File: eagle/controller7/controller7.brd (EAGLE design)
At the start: 54.7 x 47.3 mm, 70 parts, among them U1 LM75AIM, U2 MP2307, U3 MP2307, X2 ZX62D-B-5PA8

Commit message: controller6: minor changes
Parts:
- removed H1, H2, H3, H4: MOUNT-HOLE2.8, holes:2,8
- removed J1: (no value), SparkFun-Connectors:1X02_LOCK_LONGPADS
- removed J3: (no value), SparkFun-Connectors:2X5_NOSILK
- removed RTC1: DS3231M, SparkFun-DigitalIC:SOIC8
- removed U1: LM75AIM, NSC_By_element14_Batch_1.1:SOIC127P620X175-8N
- added J4: (no value), SparkFun-Connectors:1X02_LOCK_LONGPADS
- added J7: (no value), SparkFun-Connectors:2X8
- added RTC2: DS3231M, SparkFun-DigitalIC:SOIC8
- added U$2: PIZERO_THROUGH_HOLE, pizero:PIZERO_THOUGH_HOLE
- moved J2 95.6 mm to (97.8, 52.1)
- moved J5 85.1 mm to (94.0, 45.1)
- moved Q1 85.1 mm to (95.2, 35.6)
- moved Q2 85.1 mm to (95.2, 39.4)
- moved Q3 85.1 mm to (99.1, 44.5)
- moved Q4 85.1 mm to (95.2, 31.8)
- moved R10 85.1 mm to (99.1, 35.6)
- moved R11 85.1 mm to (99.1, 38.1)
- moved R12 85.1 mm to (99.1, 40.6)
- moved R13 85.1 mm to (99.1, 33.0)
- moved R14 85.1 mm to (99.1, 30.5)
- moved J8 74.7 mm to (63.5, 54.6)
- moved S1 65.9 mm to (90.2, 61.0)
- moved R5 65.6 mm to (90.2, 55.9), turned to 0 degrees
- moved J6 65.6 mm to (63.5, 44.5)
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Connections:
- removed net N$19: U$1.2, U$1.6
- removed net VBAT: J1.1, RTC1.6
- new net N$12: U$2.2, U$2.6
- new net VBAT1: J4.1, RTC2.6
- net CONV_5V: no longer J3.1
- net GND: now also J4.2, RTC2.5; no longer J1.2, J3.5, RTC1.5, U1.4
- net N$13: no longer J3.8
- net RX: no longer J3.7
- net SCL: now also RTC2.8; no longer RTC1.8, U1.2
- net SDA: now also RTC2.7; no longer RTC1.7, U1.1
- net TX: no longer J3.9
- net VCC: now also RTC2.2; no longer RTC1.2, U1.8
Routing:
- net GND: track 281.7 -> 0.00 mm, vias 9 -> 0
- net VCC: track 141.6 -> 0.00 mm, vias 6 -> 0
- net CAM_EN: track 64.3 -> 0.00 mm, vias 2 -> 0
- net SCK: track 58.6 -> 0.00 mm, vias 1 -> 0
- net BATT_VCC: track 57.6 -> 0.00 mm, vias 1 -> 0
- net CONV_3.3_INPUT: track 40.7 -> 0.00 mm, vias 2 -> 0
- net N$22: track 32.7 -> 0.00 mm
- net CAM2: track 32.2 -> 0.00 mm
- net CONV_5V: track 31.3 -> 0.00 mm, vias 1 -> 0
- net CAM3: track 24.8 -> 0.00 mm
- net SDA: track 24.3 -> 0.00 mm
- net CAM1: track 22.6 -> 0.00 mm
- net TX: track 21.8 -> 0.00 mm, vias 1 -> 0
- net CAM4: track 21.2 -> 0.00 mm, vias 2 -> 0
- net SCL: track 17.5 -> 0.00 mm
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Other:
- board size 54.7 x 47.3 mm -> 30 x 65 mm

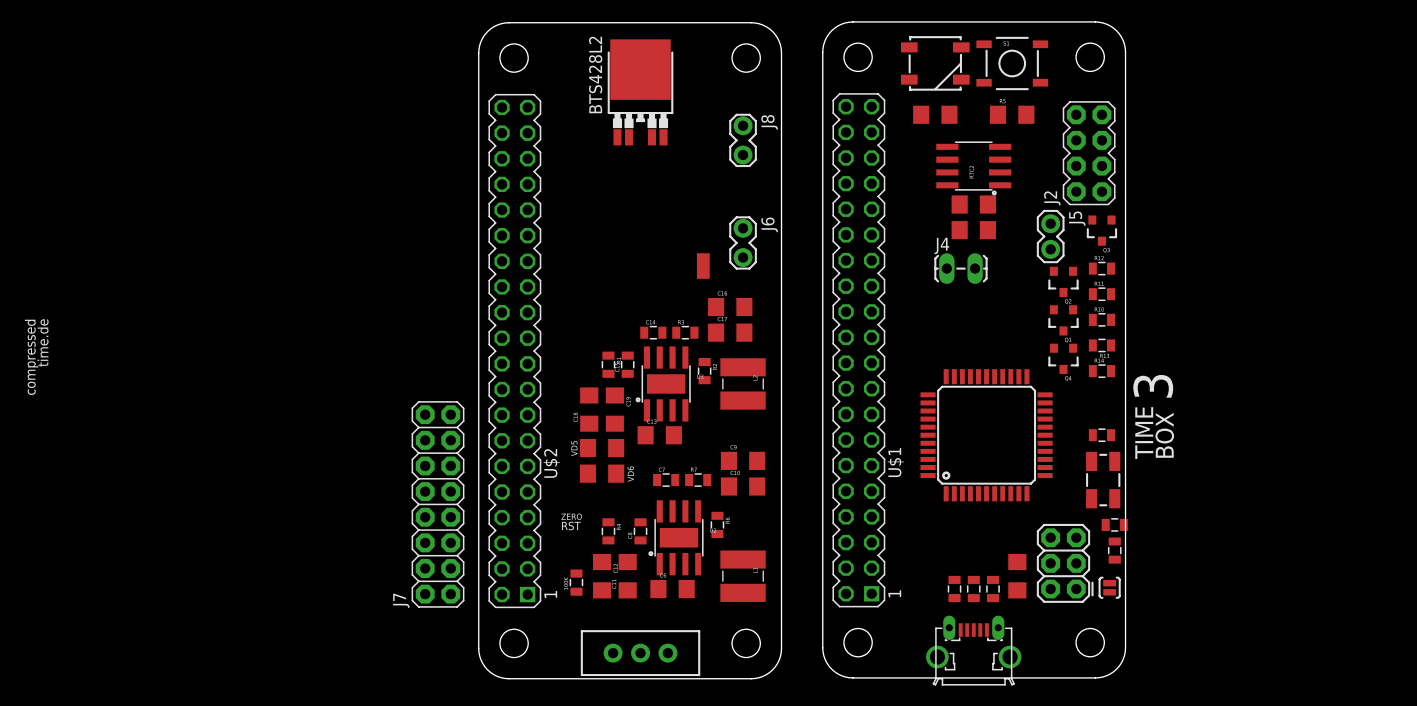
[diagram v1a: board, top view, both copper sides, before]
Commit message: controller7: profet added
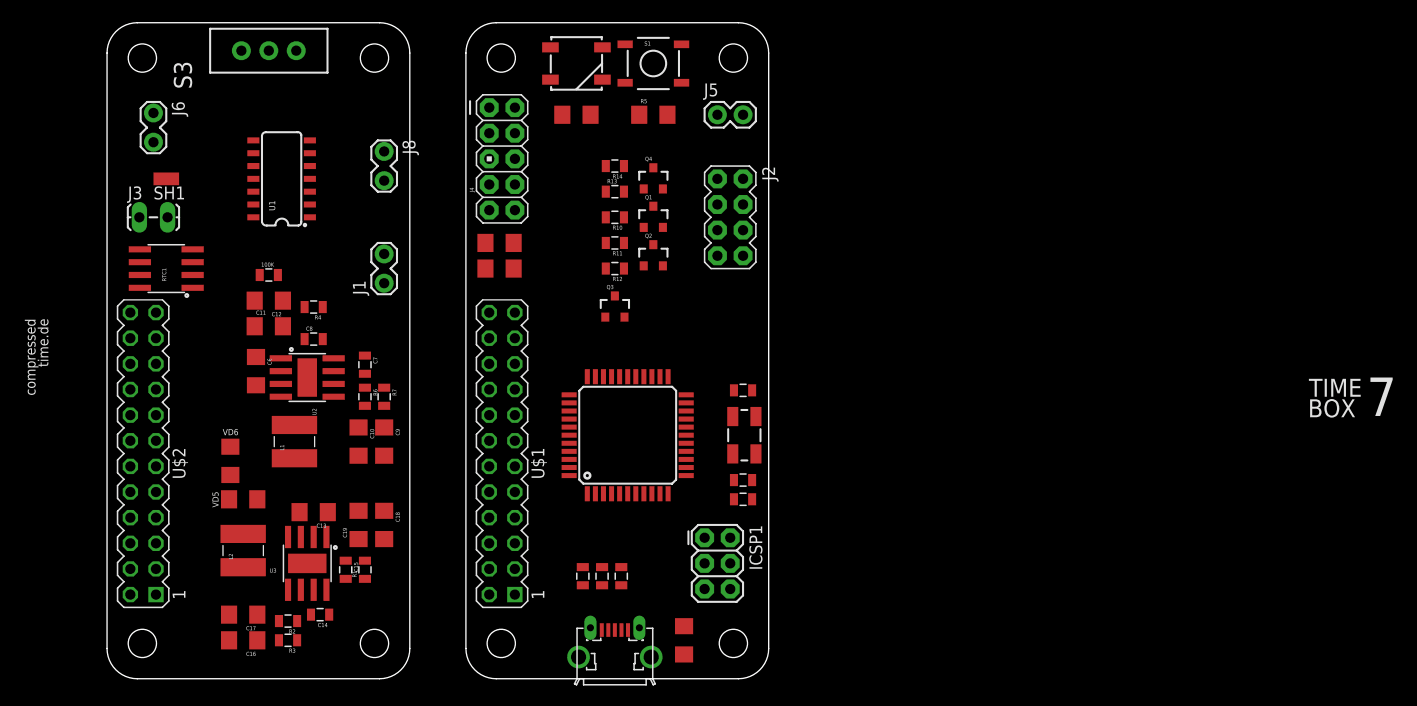
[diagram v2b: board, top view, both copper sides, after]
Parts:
- removed BTS428L2: (no value), to252:TO252-5-11
- removed ICSP: (no value), SparkFun-Connectors:2X3
- removed J7: (no value), SparkFun-Connectors:2X8
- removed JP2: (no value), SparkFun-Passives:PAD-JUMPER-2-NO_YES_SILK
- removed RTC2: DS3231M, SparkFun-DigitalIC:SOIC8
- removed S2: (no value), SparkFun-Electromechanical:SWITCH-SPDT_LOCK.007S
- removed SH: SHORT-HT5, shorts-old:SHORT_TOP-50
- added ICSP1: (no value), SparkFun-Connectors:2X3
- added J1: (no value), SparkFun-Connectors:1X02_LOCK
- added J3: (no value), SparkFun-Connectors:1X02_LOCK_LONGPADS
- added RTC1: DS3231M, SparkFun-DigitalIC:SOIC8
- added S3: (no value), SparkFun-Electromechanical:SWITCH-SPDT_LOCK.007S
- added SH1: SHORT-HT5, shorts-old:SHORT_TOP-50
- added U1: (no value), SparkFun-DigitalIC:SO14
- J4: device SparkFun-Connectors:1X02_LOCK_LONGPADS -> SparkFun-Connectors:AVR_ICSP
- U$1, U$2: value PIZERO_THROUGH_HOLE -> PIZERO_12PIN; device pizero:PIZERO_THOUGH_HOLE -> pizero:PIZERO_12PIN
- moved J6 59.5 mm to (5.08, 55.9)
- moved C16 58.5 mm to (14.0, 3.81), turned to 180 degrees
- moved C17 55.8 mm to (14.0, 6.35), turned to 180 degrees
- moved R14 52.4 mm to (50.8, 50.8), turned to 180 degrees
- moved L2 52.2 mm to (14.0, 12.7), turned to 90 degrees
- moved R13 50.6 mm to (50.8, 48.3), turned to 0 degrees
- moved R3 49.8 mm to (18.4, 3.81), turned to 180 degrees
- moved R10 49.3 mm to (50.8, 45.7), turned to 180 degrees
- moved Q3 48.9 mm to (50.8, 36.8), turned to 0 degrees
- moved R11 48.5 mm to (50.8, 43.2), turned to 180 degrees
- moved R12 48.3 mm to (50.8, 40.6), turned to 180 degrees
- moved R2 48.1 mm to (18.4, 5.71), turned to 180 degrees
- moved R8 47.4 mm to (39.4, 40.6)
- moved R9 47.0 mm to (39.4, 43.2)
- moved C6 46.6 mm to (15.2, 30.5), turned to 270 degrees
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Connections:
- removed net CAM_EN: BTS428L2.2, U$3.31
- removed net FOO1: U$3.29
- removed net N$13: JP2.1
- removed net N$39: BTS428L2.4
- removed net VBAT1: J4.1, RTC2.6
- new net CAM_EN1: U$1.20, U$3.30
- new net CAM_EN2: U$1.18, U$3.29
- new net CAM_OUT2: J1.2
- new net FOO: U$3.31
- new net GND-ISO: C10.1, C11.2, C12.1, C15.1, C16.1, C17.1, C18.2, C19.1, C8.1, C9.1, J3.2, R1.2, R2.2, R4.2, R6.2, RTC1.5, SH1.1, U$2.6, U2.4, U2.BTM, U3.4, U3.BTM, VD6.1
- new net NC: U$1.11
- new net NC_2: U$2.11
- new net PB_BUCK_EN: U$2.13, U3.7
- new net PB_CONV_5V: C16.2, C17.2, L2.P$1, R3.2, U$2.2
- new net PB_PROFET_FAULT1: U$2.21
- new net PB_PROFET_FAULT2: U$2.19
- new net PB_SCL: RTC1.8, U$2.24
- new net PB_SDA: RTC1.7, U$2.22
- new net PB_VD_DIRECT: U$2.15, VD5.1, VD6.2
- new net PROFET_FAULT1: U$1.21, U$3.27
- new net PROFET_FAULT2: U$1.19, U$3.26
- new net VBAT2: J3.1, RTC1.6
- new net VCC-ISO: C10.2, C9.2, L1.P$1, R7.2, RTC1.2
- net BATT_VCC: now also S3.1; no longer BTS428L2.TAB, S2.1
- net BUCK_EN: now also U$1.13; no longer U3.7
- net CAM_OUT: no longer BTS428L2.5
- net CONV_3.3_INPUT: now also S3.2; no longer S2.2
- net CONV_5V: now also U$1.2; no longer C16.2, C17.2, L2.P$1, R3.2
- net FOO2: now also U$1.17; no longer U$3.30
- net GND: now also ICSP1.6, U$1.6; no longer BTS428L2.1, C10.1, C11.2, C12.1, C15.1, C16.1, C17.1, C18.2, C19.1, C8.1, C9.1, ICSP.6, R1.2, R2.2, R4.2, R6.2, RTC2.5, SH.1, U2.4, U2.BTM, U3.4, U3.BTM, VD6.1
- net GNDA: now also J1.1, SH1.2; no longer SH.2
- net MISO: now also ICSP1.1; no longer ICSP.1
- net MOSI: now also ICSP1.4; no longer ICSP.4
- net N$12: now also U$1.16; no longer U$2.2, U$2.6
- net N$22: no longer S2.3
- net RST: now also ICSP1.5; no longer ICSP.5, JP2.2
- net RX: now also U$1.8
- net SCK: now also ICSP1.3; no longer ICSP.3
- net SCL: now also J4.10; no longer RTC2.8
- net SDA: now also J4.8; no longer RTC2.7
- net TX: now also U$1.10
- net VCC: now also ICSP1.2, J4.4, U$1.14; no longer C10.2, C9.2, ICSP.2, L1.P$1, R7.2, RTC2.2
- net VD_DIRECT: now also U$1.15; no longer VD5.1, VD6.2
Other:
- board text added: "7"
- board text removed: "3"
- board text removed: "RST"
- board text removed: "ZERO"

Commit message: controller7: routing power board created display board
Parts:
- removed J6, J8: (no value), SparkFun-Connectors:1X02_LOCK
- removed Q3, Q4: (no value), SparkFun-DiscreteSemi:SOT23-3
- removed RTC1: DS3231M, SparkFun-DigitalIC:SOIC8
- removed U1: (no value), SparkFun-DigitalIC:SO14
- added IC1, IC2: ILD213T, SparkFun-DiscreteSemi:SO08
- added J10, J7, J9: (no value), SparkFun-Connectors:1X02_LOCK
- added JP1: (no value), SparkFun-Passives:PAD-JUMPER-2-NO_YES_SILK
- added R15, R18, R19, R20: (no value), SparkFun-Passives:0805
- added R16, R17, R21, R22, R30: (no value), SparkFun-Passives:1206
- added RTC2: DS3231M, SparkFun-DigitalIC:SOIC8
- added RV1: (no value), SparkFun-Electromechanical:ALPS_POT
- added S2, S4, S5, S6: (no value), SparkFun-Retired:TACTILE-PTH
- added U$7: BTS7008-2EPA, SparkFun-DigitalIC:SOIC-14-PAD
- added U$8: PIZERO_12PIN, pizero:PIZERO_12PIN
- added X1: 1501_04, con-lumberg:1501_05
- C3, R11, R12, R13, R14, RUSB1, RUSB2: device SparkFun-Passives:0805 -> SparkFun-Passives:1206
- J1: device SparkFun-Connectors:1X02_LOCK -> SparkFun-Connectors:1X04_LOCK
- J3: device SparkFun-Connectors:1X02_LOCK_LONGPADS -> SparkFun-Connectors:1X04_LOCK
- J4: device SparkFun-Connectors:AVR_ICSP -> SparkFun-Connectors:1X02
- L1, L2: device SparkFun-Passives:SDR0403 -> SparkFun-Passives:SRU1038
- Q1: value (none) -> 2.5A/30V
- Q2: value (none) -> 200mA/50V
- U$2: value PIZERO_12PIN -> PIZERO_10PIN; device pizero:PIZERO_12PIN -> pizero:PIZERO_10PIN
- moved J3 81.9 mm to (84.2, 61.2)
- moved J1 59.5 mm to (84.2, 58.7), turned to 0 degrees
- moved R11 47.0 mm to (3.81, 41.9)
- moved R14 40.2 mm to (83.8, 27.9)
- moved R12 38.1 mm to (12.7, 39.4)
- moved 100K 25.0 mm to (26.7, 17.1), turned to 180 degrees
- moved C12 20.5 mm to (26.7, 19.7), turned to 0 degrees
- moved R10 18.4 mm to (63.5, 32.4)
- moved C9 17.3 mm to (14.0, 33.7), turned to 90 degrees
- moved C11 16.3 mm to (26.7, 22.2), turned to 180 degrees
- moved C18 15.3 mm to (14.0, 21.6), turned to 0 degrees
- moved R4 15.3 mm to (20.3, 21.6), turned to 0 degrees
- moved R7 14.0 mm to (14.0, 29.2), turned to 90 degrees
- moved C10 13.5 mm to (16.5, 33.7), turned to 90 degrees
- moved C16 12.8 mm to (25.4, 9.53), turned to 270 degrees
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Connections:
- removed net CAM_OUT: J8.2
- removed net CONV_3.3_INPUT: 100K.1, C11.1, C12.2, S3.2, U2.2
- removed net FOO: U$3.31
- removed net FOO2: U$1.17
- removed net PB_PROFET_FAULT1: U$2.21
- removed net PB_PROFET_FAULT2: U$2.19
- removed net PB_SCL: RTC1.8, U$2.24
- removed net PB_SDA: RTC1.7, U$2.22
- removed net PROFET_FAULT1: U$1.21, U$3.27
- removed net PROFET_FAULT2: U$1.19, U$3.26
- removed net VBAT2: J3.1, RTC1.6
- new net 3.3V: J1.2, J3.1, RV1.P$3, S2.4, S4.4, S5.4, S6.4, U$8.6
- new net ANALOG_IO: U$1.24, U$3.30
- new net BATT_VCC_RAW: J7.2, S3.1
- new net CAM_OUT1: J9.2, U$7.12, U$7.13, U$7.14
- new net DB_ANALOG_IO: RV1.P$2, U$8.24
- new net DB_BTN: S6.2, U$8.22
- new net DB_SCL: J1.3, J3.3, U$8.21
- new net DB_SDA: J1.4, J3.4, U$8.23
- new net FOO15: U$3.12
- new net FOO8: U$3.8
- new net FOOA: U$3.28
- new net N$13: IC2.3, R19.2
- new net N$15: IC1.3, R15.2
- new net N$19: IC1.1, R20.2
- new net N$34: IC1.5, IC1.7, IC2.5, IC2.7, J2.7, JP1.2, X1.1
- new net N$35: J2.8, Q1.3
- new net N$36: Q1.1, Q2.2, R10.1
- new net N$37: J1.1
- new net N$38: R14.1, S5.2
- new net N$39: R30.2, S4.2
- new net N$40: R21.2, S2.2
- new net N$43: R22.2, RV1.P$1
- new net PB_CAM_EN1: R11.1, U$2.20, U$7.2
- new net PB_CAM_EN2: R12.2, U$2.15, U$7.6
- new net PB_PROFET_1: R17.1, U$2.18, U$7.3
- new net PB_PROFET_2: U$2.19, U$7.4
- new net PB_PROFET_3: R16.2, U$2.17, U$7.5
- new net PROFET1: U$1.18, U$3.37
- new net PROFET2: U$1.19, U$3.38
- new net PROFET3: U$1.17, U$3.39
- new net SWITCH_USB_VCC: Q2.1, U$3.22
- new net VBAT1: J4.1, RTC2.6
- new net VCC_2: R14.2, R21.1, R22.1, R30.1, U$8.14
- net BATT_VCC: now also 100K.1, C11.1, C12.2, S3.2, U$7.P$1, U$7.P$2, U$7.VS, U2.2; no longer J6.2, S3.1
- net BTN: now also U$1.22, U$3.32; no longer U$3.36
- net BUCK_EN: now also U$1.16, U$3.1; no longer U$1.13, U$3.12
- net CAM1: now also R20.1, U$3.29; no longer Q1.1, R10.2, U$3.40
- net CAM2: now also R15.1, U$3.27; no longer Q2.1, R11.2, U$3.39
- net CAM3: now also R18.1, U$3.26; no longer Q3.1, R12.2, U$3.38
- net CAM4: now also R19.1, U$3.25; no longer Q4.1, R13.1, U$3.37
- net CAM_EN1: now also U$3.36; no longer U$3.30
- net CAM_EN2: now also U$1.15, U$3.40; no longer U$1.18, U$3.29
- net CAM_OUT2: now also J10.2, U$7.10, U$7.8, U$7.9; no longer J1.2
- net CONV_5V: now also Q1.2, R10.2
- net GND: now also IC1.2, IC1.4, IC2.2, IC2.4, JP1.1, Q2.3, RTC2.5; no longer J2.7, Q1.2, Q2.2, Q3.2, R14.1
- net GND-ISO: now also R11.2, R12.1, R16.1, R17.2, U$7.1, U2.P$1, U3.P$1; no longer J3.2, RTC1.5
- net GNDA: now also J10.1, J7.1, J9.1; no longer J1.1, J6.1, J8.1
- net LED: now also U$3.31; no longer U$3.32
- net N$12: now also IC2.1, R18.2; no longer U$1.16
- net N$16: no longer Q4.3
- net N$17: now also L1.2; no longer L1.P$2
- net N$18: now also IC1.8, R13.1; no longer Q4.2, R14.2
- net N$26: now also L2.2; no longer L2.P$2
- net N$31: now also IC1.6, X1.3; no longer Q1.3, R10.1
- net N$32: now also IC2.8, X1.2; no longer Q2.3, R11.1
- net N$33: now also IC2.6; no longer Q3.3, R12.1
- net PB_BUCK_EN: now also U$2.16; no longer U$2.13
- net PB_CONV_5V: now also L2.1; no longer L2.P$1
- net PB_VD_DIRECT: now also U$2.13; no longer U$2.15
- net SCL: now also RTC2.8, U$1.21; no longer J4.10
- net SDA: now also RTC2.7, U$1.23; no longer J4.8
- net VCC: now also RTC2.2; no longer J4.4
- net VCC-ISO: now also L1.1, U$2.14; no longer L1.P$1, RTC1.2
- net VD_DIRECT: now also U$1.13; no longer U$1.15
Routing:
- net GND: track 0.00 -> 155.0 mm, vias 0 -> 3
- net GND-ISO: track 0.00 -> 148.9 mm
- net VCC: track 0.00 -> 130.7 mm, vias 0 -> 8
- net BATT_VCC: track 0.00 -> 95.6 mm, vias 0 -> 1
- net BTN: track 0.00 -> 52.5 mm, vias 0 -> 2
- net N$34: track 0.00 -> 45.5 mm
- net SDA: track 0.00 -> 44.5 mm, vias 0 -> 2
- net CONV_5V: track 0.00 -> 43.7 mm, vias 0 -> 2
- net SCL: track 0.00 -> 41.5 mm, vias 0 -> 2
- net GNDA: track 0.00 -> 39.8 mm
- net N$16: track 0.00 -> 34.8 mm, vias 0 -> 1
- net PB_CONV_5V: track 0.00 -> 32.5 mm
- net PB_BUCK_EN: track 0.00 -> 30.1 mm, vias 0 -> 1
- net RX: track 0.00 -> 28.1 mm, vias 0 -> 2
- net PB_PROFET_1: track 0.00 -> 28.0 mm
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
